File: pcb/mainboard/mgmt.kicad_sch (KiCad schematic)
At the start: 98 parts, among them J10 FAN_01, J11 XILINX_JTAG, J12 JUMPER_0402_SPDT, J13 JUMPER_0402_SPDT, J14 RJ45, J15 PMOD_HOST, J48 CONN_01X10, J8 FAN_01, J9 CONN_01X03, U23 STM32H735-UFBGA176-25, U24 AT24MAC402, U25 ADM3101E_QFN, U31 ECS-1612MV-250-CN, U32 S25FL128SAGBHIA10, U8 XC7K70T-2FBG484C

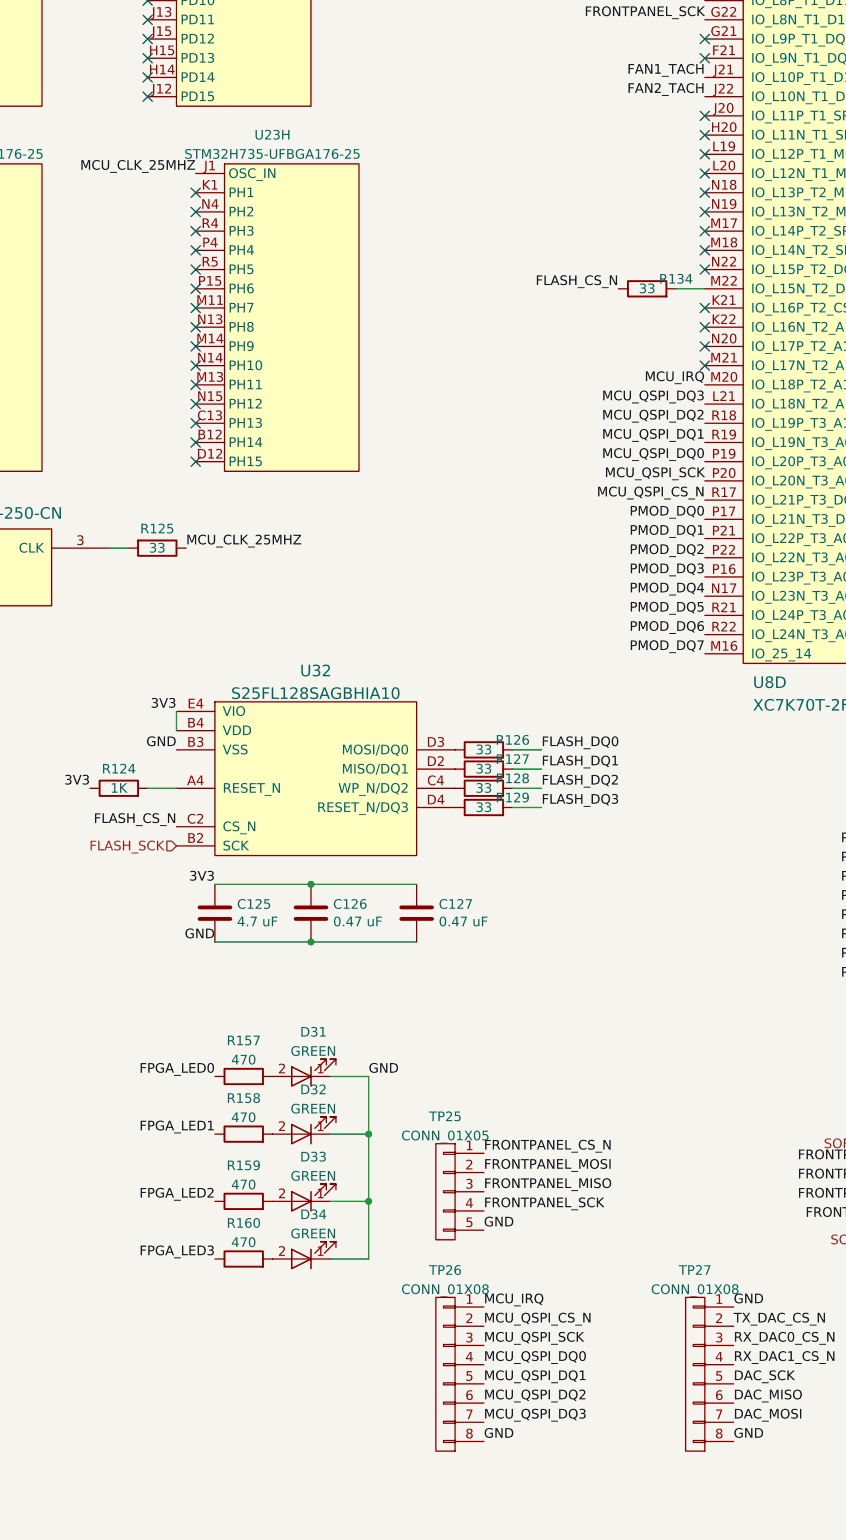
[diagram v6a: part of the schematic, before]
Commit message: Initial floorplanning work, added SFP+ LEDs
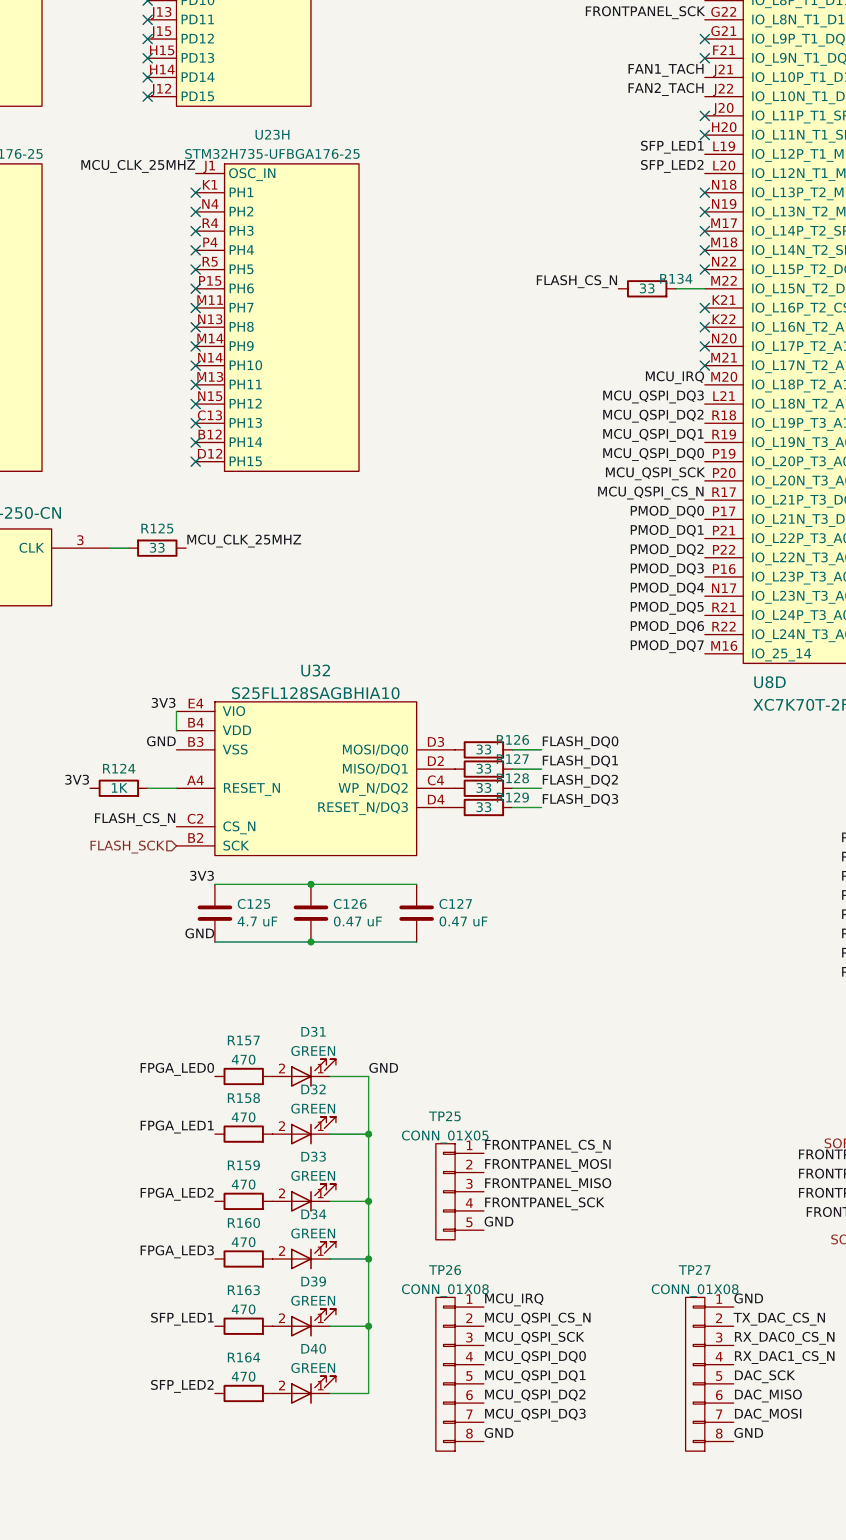
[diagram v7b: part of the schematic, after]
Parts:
- added D39, D40: GREEN, azonenberg_pcb:EIA_0603_LED, symbol device:LED
- added R163, R164: 470, azonenberg_pcb:EIA_0402_RES_NOSILK, symbol device:R
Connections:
- net GND: now also D39.1 (K), D40.1 (K)
- net SFP_LED1: now reaches U8.L19 (IO_L12P_T1_MRCC_14)
- net SFP_LED1: now also R163.1
- net SFP_LED2: now reaches U8.L20 (IO_L12N_T1_MRCC_14)
- net SFP_LED2: now also R164.1
- new net: D39.2 (A), R163.2
- new net: D40.2 (A), R164.2
- no-connect marks 116 -> 114
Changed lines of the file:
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@@
   (junction (at 97.79 99.06) (diameter 0) (color 0 0 0 0)
   )
+  (junction (at 309.88 224.79) (diameter 0) (color 0 0 0 0)
+  )
   (junction (at 309.88 217.17) (diameter 0) (color 0 0 0 0)
   )
   (junction (at 302.26 182.88) (diameter 0) (color 0 0 0 0)
   )
+  (junction (at 309.88 233.68) (diameter 0) (color 0 0 0 0)
+  )
   (junction (at 45.72 104.14) (diameter 0) (color 0 0 0 0)
   )
@@
   (no_connect (at 245.11 45.72))
   (no_connect (at 245.11 119.38))
-  (no_connect (at 354.33 81.28))
   (no_connect (at 152.4 111.76))
   (no_connect (at 287.02 104.14))
@@
   (no_connect (at 354.33 50.8))
   (no_connect (at 245.11 96.52))
-  (no_connect (at 354.33 78.74))
   (no_connect (at 245.11 66.04))
   (no_connect (at 245.11 50.8))
@@
     (stroke (width 0) (type default) (color 0 0 0 0))
   )
+  (wire (pts (xy 304.8 233.68) (xy 309.88 233.68))
+    (stroke (width 0) (type default) (color 0 0 0 0))
+  )
   (wire (pts (xy 350.52 25.4) (xy 354.33 25.4))
     (stroke (width 0) (type default) (color 0 0 0 0))
@@
     (stroke (width 0) (type default) (color 0 0 0 0))
   )
+  (wire (pts (xy 309.88 242.57) (xy 304.8 242.57))
+    (stroke (width 0) (type default) (color 0 0 0 0))
+  )
   (wire (pts (xy 45.72 111.76) (xy 57.15 111.76))
     (stroke (width 0) (type default) (color 0 0 0 0))
@@
     (stroke (width 0) (type default) (color 0 0 0 0))
   )
+  (wire (pts (xy 309.88 233.68) (xy 309.88 224.79))
+    (stroke (width 0) (type default) (color 0 0 0 0))
+  )
   (wire (pts (xy 132.08 45.72) (xy 132.08 48.26))
     (stroke (width 0) (type default) (color 0 0 0 0))
@@
     (stroke (width 0) (type default) (color 0 0 0 0))
   )
+  (wire (pts (xy 309.88 233.68) (xy 309.88 242.57))
+    (stroke (width 0) (type default) (color 0 0 0 0))
+  )
   (wire (pts (xy 350.52 30.48) (xy 354.33 30.48))
     (stroke (width 0) (type default) (color 0 0 0 0))
@@
     (effects (font (size 1.27 1.27)) (justify right bottom))
   )
+  (label "SFP_LED2" (at 354.33 81.28 180)
+    (effects (font (size 1.27 1.27)) (justify right bottom))
+  )
   (label "PMOD_DQ3" (at 354.33 134.62 180)
     (effects (font (size 1.27 1.27)) (justify right bottom))
@@
     (effects (font (size 1.27 1.27)) (justify right bottom))
   )
+  (label "SFP_LED2" (at 289.56 242.57 180)
+    (effects (font (size 1.27 1.27)) (justify right bottom))
+  )
   (label "DAC_SCK" (at 358.14 241.3 0)
     (effects (font (size 1.27 1.27)) (justify left bottom))
@@
     (effects (font (size 1.27 1.27)) (justify right bottom))
   )
+  (label "SFP_LED1" (at 289.56 233.68 180)
+    (effects (font (size 1.27 1.27)) (justify right bottom))
+  )
   (label "3V3" (at 382.27 157.48 180)
     (effects (font (size 1.27 1.27)) (justify right bottom))
@@
     (effects (font (size 1.27 1.27)) (justify right bottom))
   )
+  (label "SFP_LED1" (at 354.33 78.74 180)
+    (effects (font (size 1.27 1.27)) (justify right bottom))
+  )
   (label "MCU_QSPI_DQ2" (at 354.33 114.3 180)
     (effects (font (size 1.27 1.27)) (justify right bottom))
@@
     (pin "2")
   )
+  (symbol (lib_id "device:LED") (at 300.99 233.68 180) (unit 1)
+    (in_bom yes) (on_board yes) (fields_autoplaced)
+    (property "Reference" "D39" (id 0) (at 302.5902 227.8212 0))
+    (property "Value" "GREEN" (id 1) (at 302.5902 230.3581 0))
+    (property "Footprint" "azonenberg_pcb:EIA_0603_LED" (id 2) (at 300.99 233.68 0)
+      (effects (font (size 1.27 1.27)) hide)
+    )
+    (property "Datasheet" "" (id 3) (at 300.99 233.68 0)
+      (effects (font (size 1.27 1.27)) hide)
+    )
+    (pin "1")
+    (pin "2")
+  )
   (symbol (lib_id "device:C") (at 77.47 39.37 0) (unit 1)
     (in_bom yes) (on_board yes) (fields_autoplaced)
@@
     (pin "2")
   )
+  (symbol (lib_id "device:R") (at 293.37 233.68 90) (unit 1)
+    (in_bom yes) (on_board yes) (fields_autoplaced)
+    (property "Reference" "R163" (id 0) (at 293.37 228.9642 90))
+    (property "Value" "470" (id 1) (at 293.37 231.5011 90))
+    (property "Footprint" "azonenberg_pcb:EIA_0402_RES_NOSILK" (id 2) (at 293.37 235.458 90)
+      (effects (font (size 1.27 1.27)) hide)
+    )
+    (property "Datasheet" "" (id 3) (at 293.37 233.68 0)
+      (effects (font (size 1.27 1.27)) hide)
+    )
+    (pin "1")
+    (pin "2")
+  )
   (symbol (lib_id "device:C") (at 40.64 171.45 0) (unit 1)
     (in_bom yes) (on_board yes) (fields_autoplaced)
@@
     (pin "3")
   )
+  (symbol (lib_id "device:R") (at 293.37 242.57 90) (unit 1)
+    (in_bom yes) (on_board yes) (fields_autoplaced)
+    (property "Reference" "R164" (id 0) (at 293.37 237.8542 90))
+    (property "Value" "470" (id 1) (at 293.37 240.3911 90))
+    (property "Footprint" "azonenberg_pcb:EIA_0402_RES_NOSILK" (id 2) (at 293.37 244.348 90)
+      (effects (font (size 1.27 1.27)) hide)
+    )
+    (property "Datasheet" "" (id 3) (at 293.37 242.57 0)
+      (effects (font (size 1.27 1.27)) hide)
+    )
+    (pin "1")
+    (pin "2")
+  )
   (symbol (lib_id "device:C") (at 41.91 154.94 0) (unit 1)
     (in_bom yes) (on_board yes) (fields_autoplaced)
@@
       (effects (font (size 1.27 1.27)) hide)
     )
+    (pin "1")
+    (pin "2")
+  )
+  (symbol (lib_id "device:LED") (at 300.99 242.57 180) (unit 1)
+    (in_bom yes) (on_board yes) (fields_autoplaced)
+    (property "Reference" "D40" (id 0) (at 302.5902 236.7112 0))
+    (property "Value" "GREEN" (id 1) (at 302.5902 239.2481 0))
+    (property "Footprint" "azonenberg_pcb:EIA_0603_LED" (id 2) (at 300.99 242.57 0)
+      (effects (font (size 1.27 1.27)) hide)
+    )
+    (property "Datasheet" "" (id 3) (at 300.99 242.57 0)
+      (effects (font (size 1.27 1.27)) hide)
+    )
